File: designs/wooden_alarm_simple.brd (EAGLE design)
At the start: 49.4 x 53 mm, 16 parts, among them IC1 ESP-12E/F

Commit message: printready alarm simple layout
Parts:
- moved VCC 15.1 mm to (17.2, 5.60)
- moved IO_0_SWITCH 5.23 mm to (9.96, 12.7)
- moved R3 4.84 mm to (42.6, 15.2)
- moved R4 4.57 mm to (42.6, 34.6), turned to 0 degrees
- moved IO_15_SWITCH 4.42 mm to (35.6, 12.6)
- moved R5 4.20 mm to (19.4, 14.2), turned to 180 degrees
- moved IO_2_SWITCH 3.60 mm to (43.4, 28.0)
- moved JUMPER_CLK 3.06 mm to (15.6, 23.5)
- moved IC1 2.60 mm to (27.9, 27.9)
- moved RXTX 2.53 mm to (41.5, 43.3)
- moved JUMPER_RTC 1.80 mm to (28.7, 47.0)
- moved R1 1.52 mm to (8.76, 33.7)
- moved C1 1.41 mm to (8.75, 47.4)
- moved R2 1.40 mm to (8.76, 38.1)
- moved JUMPER_TOUCH 0.89 mm to (7.64, 25.0)
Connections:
- net GND: now also JUMPER_CLK.2; no longer JUMPER_CLK.1
- net VCC: now also JUMPER_CLK.1; no longer JUMPER_CLK.2
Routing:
- net VCC: track 123.9 -> 152.2 mm, vias 2 -> 0
- net N$3: track 11.9 -> 18.6 mm
- net SQW: track 22.2 -> 26.9 mm
- net N$7: track 4.32 -> 8.99 mm
- net SWITCH_PIN: track 15.7 -> 20.0 mm
- net SDA: track 19.2 -> 22.4 mm
- net TX: track 7.59 -> 10.7 mm
- net RX: track 7.05 -> 10.2 mm
- net N$1: track 9.41 -> 11.9 mm
- net N$5: track 3.67 -> 6.07 mm
- net EN: track 9.49 -> 11.7 mm
- net SCL: track 16.1 -> 18.1 mm
- net TOUCH_IO: track 14.4 -> 15.1 mm
- net CLK_DISPLAY: track 5.57 -> 4.91 mm
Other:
- board text added: "GND VCC"
- board text added: "GND VCC DIO CLK"
- board text added: "GND VCC SQW SCL SDA"
- board text added: "GND VCC TOUCH"
- board text added: "v1.0"
- board text removed: "A"

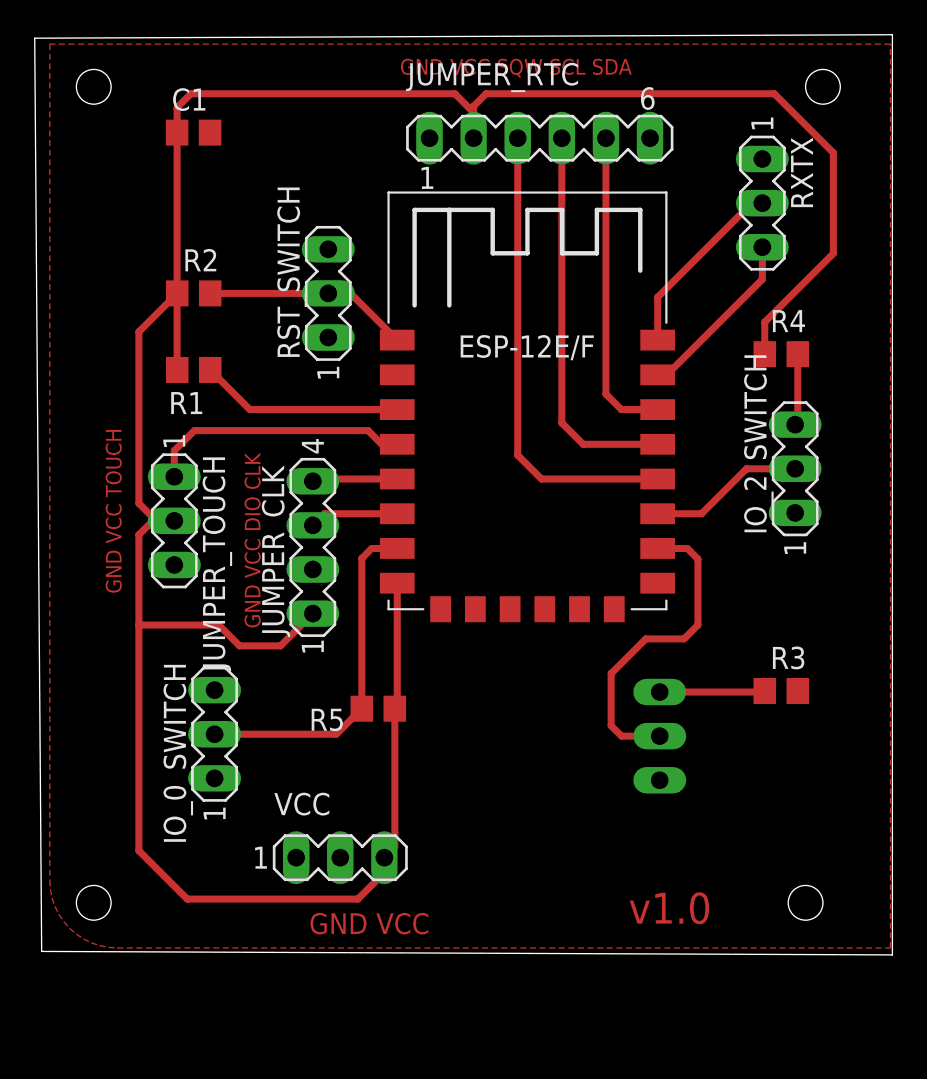
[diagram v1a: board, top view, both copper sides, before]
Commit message: updated layout and pdf for etching
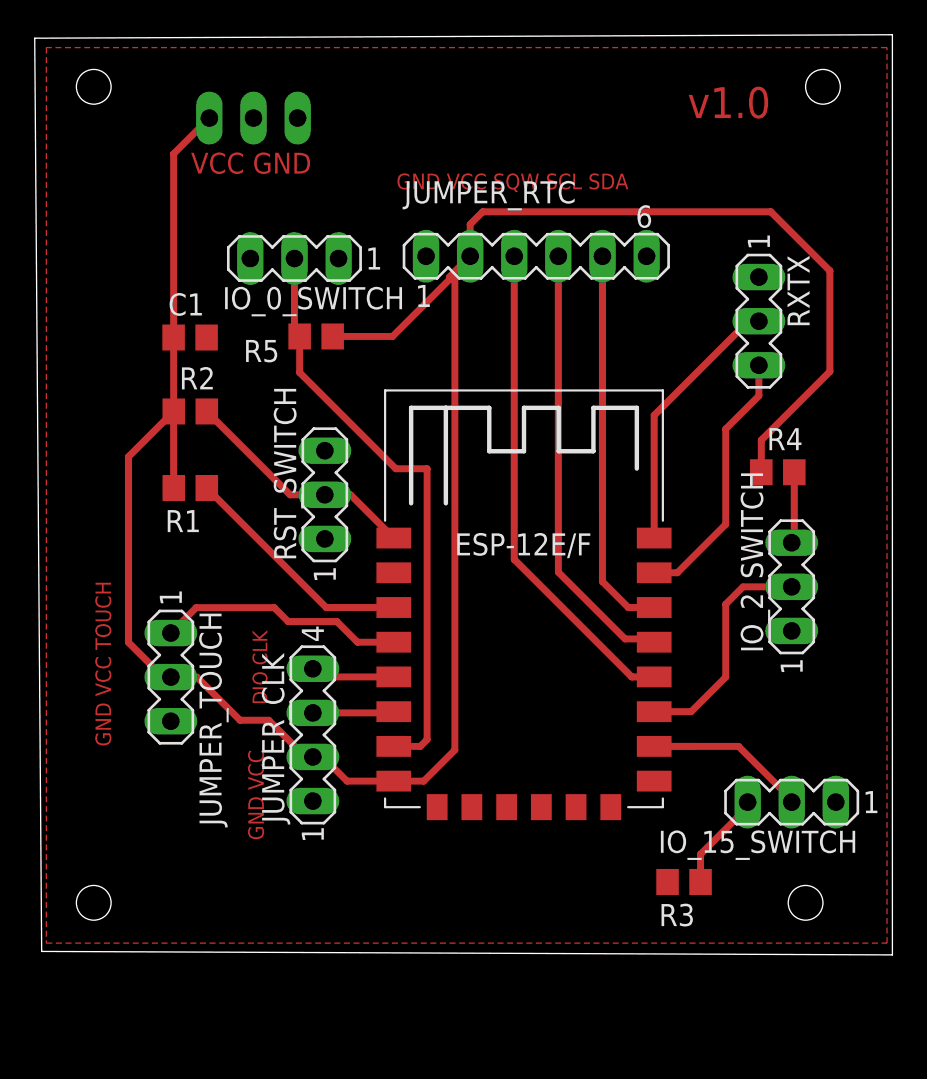
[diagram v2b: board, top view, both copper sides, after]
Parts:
- moved VCC 42.9 mm to (12.2, 48.2), flipped to the bottom
- moved IO_0_SWITCH 27.8 mm to (14.6, 40.1), turned to 180 degrees
- moved R5 21.7 mm to (15.8, 35.6)
- moved R3 12.3 mm to (37.0, 4.20), turned to 180 degrees
- moved C1 11.8 mm to (8.55, 35.6)
- moved RST_SWITCH 11.6 mm to (16.3, 26.5)
- moved IC1 11.4 mm to (27.7, 16.5)
- moved JUMPER_CLK 10.8 mm to (15.6, 12.7)
- moved JUMPER_TOUCH 9.00 mm to (7.44, 16.0)
- moved IO_15_SWITCH 8.50 mm to (43.2, 8.80), flipped to the top, turned to 180 degrees
- moved IO_2_SWITCH 6.80 mm to (43.2, 21.2)
- moved R2 6.80 mm to (8.56, 31.3)
- moved R4 6.80 mm to (42.4, 27.8)
- moved JUMPER_RTC 6.80 mm to (28.5, 40.2)
- moved R1 6.80 mm to (8.56, 26.9)
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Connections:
- net GND: now also JUMPER_CLK.1, VCC.1; no longer JUMPER_CLK.2
- net VCC: now also JUMPER_CLK.2; no longer JUMPER_CLK.1
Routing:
- net VCC: track 152.2 -> 135.6 mm
- net SWITCH_PIN: track 20.0 -> 34.0 mm
- net N$3: track 18.6 -> 9.34 mm
- net RX: track 10.2 -> 15.2 mm
- net TX: track 10.7 -> 15.3 mm
- net N$7: track 8.99 -> 13.4 mm
- net SCL: track 18.1 -> 22.3 mm
- net SDA: track 22.4 -> 25.4 mm
- net EN: track 11.7 -> 13.6 mm
- net N$1: track 11.9 -> 13.8 mm
- net SQW: track 26.9 -> 28.3 mm
- net TOUCH_IO: track 15.1 -> 14.3 mm
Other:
- board text added: "DIO CLK"
- board text added: "VCC GND"
